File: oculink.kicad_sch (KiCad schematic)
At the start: 15 parts, among them J6 OCuLink_x4_Amphenol_G14A42121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

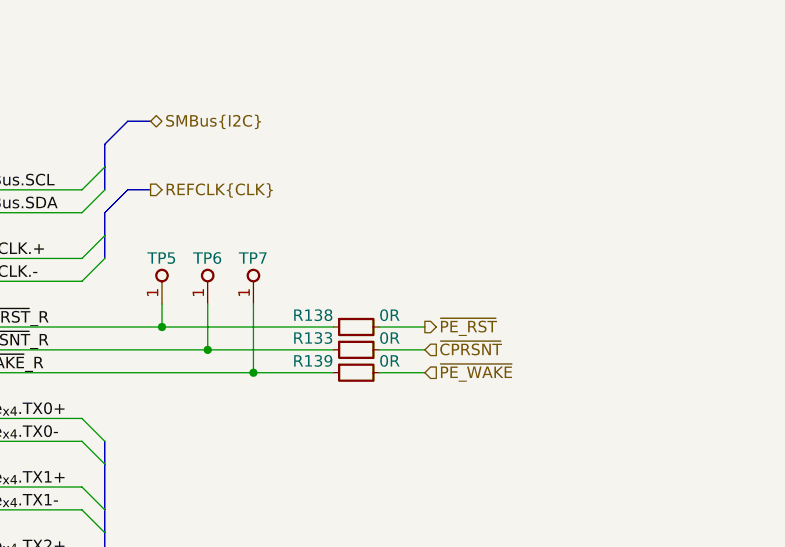
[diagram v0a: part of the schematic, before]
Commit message: [#85196] WIP: Add power sequencing, connect CPRSNT signal
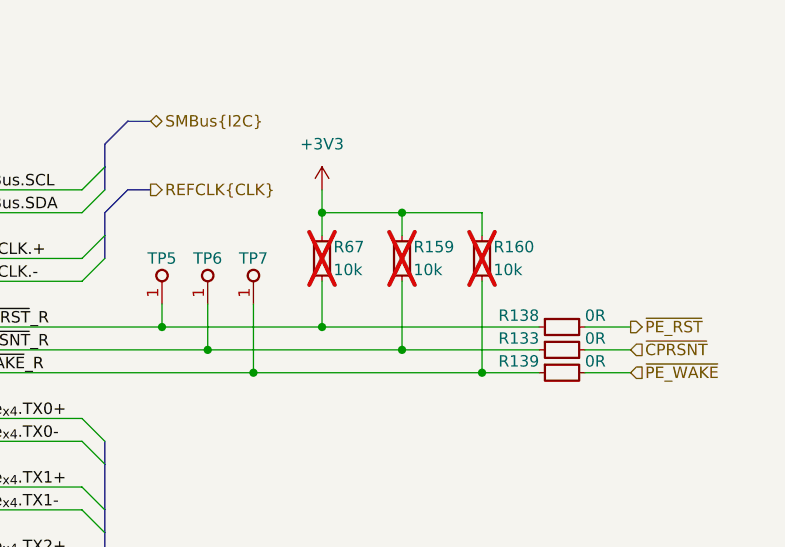
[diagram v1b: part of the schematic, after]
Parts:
- added R159, R160, R67: R_10k_0402, antmicro-footprints:R_0402_1005Metric, symbol antmicroResistors0402:R_10k_0402
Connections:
- net ~{CPRSNT}_R: now also R159.1
- net ~{CWAKE}_R: now also R160.1
- net ~{PE_ RST}_R: now also R67.1
- new net +3V3: R159.2, R160.2, R67.2
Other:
- moved on the sheet: R133, R138, R139

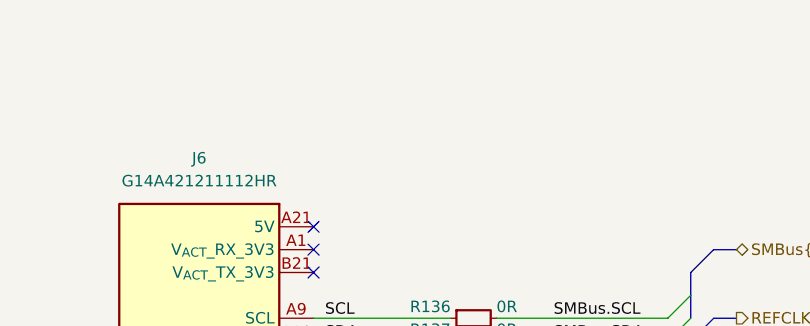
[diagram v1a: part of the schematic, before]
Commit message: [#85196] Clear ERC, minor schematic fixes
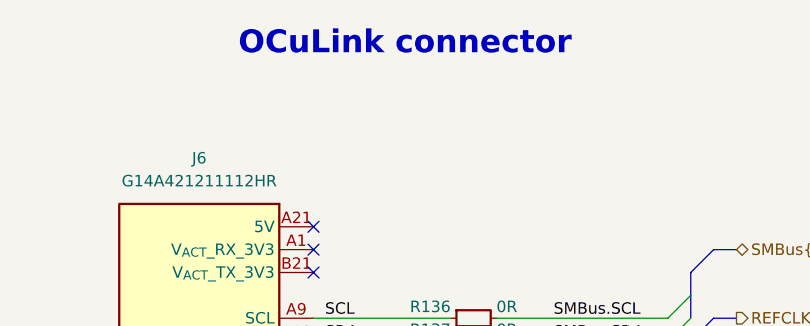
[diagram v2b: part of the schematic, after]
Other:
- note added: "OCuLink connector"
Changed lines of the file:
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@@
 		(comment 1 "www.antmicro.com")
+	)
+	(text "OCuLink connector"
+		(exclude_from_sim no)
+		(at 201.93 64.77 0)
+		(effects
+			(font
+				(size 2.54 2.54)
+				(thickness 0.508)
+				(bold yes)
+			)
+		)
 	)
 	(junction

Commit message: [#85196] Re-annotate schematic
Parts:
- renumbered D1 to D4, D3 to D6, D4 to D7, D2 to D8, D6 to D9, J6 to J9, R136 to R162, R137 to R163, R67 to R164, R159 to R165, R160 to R166, R138 to R167, R133 to R168, R139 to R169, TP5 to TP14, TP6 to TP15, TP7 to TP16
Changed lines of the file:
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@@
 		(on_board yes)
 		(dnp yes)
-		(property "Reference" "R160"
+		(property "Reference" "R166"
 			(at 276.86 101.6 90)
 			(effects
@@
 			(project "10-gbe-expansion"
 				(path "/04bda987-e5eb-48b4-9e90-d8211dc11b39/0cbe4665-19ed-43d5-9283-363c2bb680b6"
-					(reference "R160")
+					(reference "R166")
 					(unit 1)
 				)
@@
 		(dnp no)
 		(fields_autoplaced yes)
-		(property "Reference" "D2"
+		(property "Reference" "D8"
 			(at 222.25 238.76 0)
 			(effects
@@
 			(project "10-gbe-expansion"
 				(path "/04bda987-e5eb-48b4-9e90-d8211dc11b39/0cbe4665-19ed-43d5-9283-363c2bb680b6"
-					(reference "D2")
+					(reference "D8")
 					(unit 1)
 				)
@@
 		(on_board yes)
 		(dnp no)
-		(property "Reference" "R139"
+		(property "Reference" "R169"
 			(at 281.94 114.3 0)
 			(effects
@@
 			(project ""
 				(path "/04bda987-e5eb-48b4-9e90-d8211dc11b39/0cbe4665-19ed-43d5-9283-363c2bb680b6"
-					(reference "R139")
+					(reference "R169")
 					(unit 1)
 				)
@@
 		(on_board yes)
 		(dnp no)
-		(property "Reference" "R136"
+		(property "Reference" "R162"
 			(at 207.01 93.98 0)
 			(effects
@@
 			(project "10-gbe-expansion"
 				(path "/04bda987-e5eb-48b4-9e90-d8211dc11b39/0cbe4665-19ed-43d5-9283-363c2bb680b6"
-					(reference "R136")
+					(reference "R162")
 					(unit 1)
 				)
@@
 		(dnp no)
 		(fields_autoplaced yes)
-		(property "Reference" "D6"
+		(property "Reference" "D9"
 			(at 271.78 238.76 0)
 			(effects
@@
 			(project "10-gbe-expansion"
 				(path "/04bda987-e5eb-48b4-9e90-d8211dc11b39/0cbe4665-19ed-43d5-9283-363c2bb680b6"
-					(reference "D6")
+					(reference "D9")
 					(unit 1)
 				)
@@
 		(on_board yes)
 		(dnp yes)
-		(property "Reference" "R67"
+		(property "Reference" "R164"
 			(at 259.08 101.6 90)
 			(effects
@@
 			(project ""
 				(path "/04bda987-e5eb-48b4-9e90-d8211dc11b39/0cbe4665-19ed-43d5-9283-363c2bb680b6"
-					(reference "R67")
+					(reference "R164")
 					(unit 1)
 				)
@@
 		(on_board yes)
 		(dnp no)
-		(property "Reference" "#PWR0268"
+		(property "Reference" "#PWR0322"
 			(at 167.64 224.79 0)
 			(effects
@@
 			(project "10-gbe-expansion"
 				(path "/04bda987-e5eb-48b4-9e90-d8211dc11b39/0cbe4665-19ed-43d5-9283-363c2bb680b6"
-					(reference "#PWR0268")
+					(reference "#PWR0322")
 					(unit 1)
 				)
@@
 		(dnp no)
 		(fields_autoplaced yes)
-		(property "Reference" "D1"
+		(property "Reference" "D4"
 			(at 171.45 213.36 0)
 			(effects
@@
 			(project "10-gbe-expansion"
 				(path "/04bda987-e5eb-48b4-9e90-d8211dc11b39/0cbe4665-19ed-43d5-9283-363c2bb680b6"
-					(reference "D1")
+					(reference "D4")
 					(unit 1)
 				)
@@
 		(dnp no)
 		(fields_autoplaced yes)
-		(property "Reference" "#PWR0315"
+		(property "Reference" "#PWR0320"
 			(at 273.05 95.25 0)
 			(effects
@@
 			(project ""
 				(path "/04bda987-e5eb-48b4-9e90-d8211dc11b39/0cbe4665-19ed-43d5-9283-363c2bb680b6"
-					(reference "#PWR0315")
+					(reference "#PWR0320")
 					(unit 1)
 				)
@@
 		(on_board yes)
 		(dnp no)
-		(property "Reference" "#PWR0270"
+		(property "Reference" "#PWR0324"
 			(at 267.97 224.79 0)
 			(effects
@@
 			(project "10-gbe-expansion"
 				(path "/04bda987-e5eb-48b4-9e90-d8211dc11b39/0cbe4665-19ed-43d5-9283-363c2bb680b6"
-					(reference "#PWR0270")
+					(reference "#PWR0324")
 					(unit 1)
 				)
@@
 		(dnp no)
 		(fields_autoplaced yes)
-		(property "Reference" "D3"
+		(property "Reference" "D6"
 			(at 271.78 213.36 0)
 			(effects
@@
 			(project "10-gbe-expansion"
 				(path "/04bda987-e5eb-48b4-9e90-d8211dc11b39/0cbe4665-19ed-43d5-9283-363c2bb680b6"
-					(reference "D3")
+					(reference "D6")
 					(unit 1)
 				)
@@
 		(on_board yes)
 		(dnp no)
-		(property "Reference" "TP5"
+		(property "Reference" "TP14"
 			(at 240.03 102.87 90)
 			(effects
@@
 			(project ""
 				(path "/04bda987-e5eb-48b4-9e90-d8211dc11b39/0cbe4665-19ed-43d5-9283-363c2bb680b6"
-					(reference "TP5")
+					(reference "TP14")
 					(unit 1)
 				)
@@
 		(dnp no)
 		(fields_autoplaced yes)
-		(property "Reference" "J6"
+		(property "Reference" "J9"
 			(at 179.07 77.47 0)
 			(effects
@@
 			(project ""
 				(path "/04bda987-e5eb-48b4-9e90-d8211dc11b39/0cbe4665-19ed-43d5-9283-363c2bb680b6"
-					(reference "J6")
+					(reference "J9")
 					(unit 1)
 				)
@@
 		(on_board yes)
 		(dnp no)
-		(property "Reference" "#PWR0271"
+		(property "Reference" "#PWR0321"
 			(at 172.72 181.61 0)
 			(effects
@@
 			(project "10-gbe-expansion"
 				(path "/04bda987-e5eb-48b4-9e90-d8211dc11b39/0cbe4665-19ed-43d5-9283-363c2bb680b6"
-					(reference "#PWR0271")
+					(reference "#PWR0321")
 					(unit 1)
 				)
@@
 		(on_board yes)
 		(dnp no)
-		(property "Reference" "R137"
+		(property "Reference" "R163"
 			(at 207.01 96.52 0)
 			(effects
@@
 			(project "10-gbe-expansion"
 				(path "/04bda987-e5eb-48b4-9e90-d8211dc11b39/0cbe4665-19ed-43d5-9283-363c2bb680b6"
-					(reference "R137")
+					(reference "R163")
 					(unit 1)
 				)
@@
 		(on_board yes)
 		(dnp no)
-		(property "Reference" "R138"
+		(property "Reference" "R167"
 			(at 281.94 109.22 0)
 			(effects
@@
 			(project "10-gbe-expansion"
 				(path "/04bda987-e5eb-48b4-9e90-d8211dc11b39/0cbe4665-19ed-43d5-9283-363c2bb680b6"
-					(reference "R138")
+					(reference "R167")
 					(unit 1)
 				)
@@
 		(on_board yes)
 		(dnp no)
-		(property "Reference" "#PWR0269"
+		(property "Reference" "#PWR0326"
 			(at 218.44 250.19 0)
 			(effects
@@
 			(project "10-gbe-expansion"
 				(path "/04bda987-e5eb-48b4-9e90-d8211dc11b39/0cbe4665-19ed-43d5-9283-363c2bb680b6"
-					(reference "#PWR0269")
+					(reference "#PWR0326")
 					(unit 1)
 				)
@@
 		(on_board yes)
 		(dnp no)
-		(property "Reference" "TP6"
+		(property "Reference" "TP15"
 			(at 245.11 102.87 90)
 			(effects
@@
 			(project "10-gbe-expansion"
 				(path "/04bda987-e5eb-48b4-9e90-d8211dc11b39/0cbe4665-19ed-43d5-9283-363c2bb680b6"
-					(reference "TP6")
+					(reference "TP15")
 					(unit 1)
 				)
@@
 		(on_board yes)
 		(dnp no)
-		(property "Reference" "#PWR0274"
+		(property "Reference" "#PWR0327"
 			(at 267.97 250.19 0)
 			(effects
@@
 			(project "10-gbe-expansion"
 				(path "/04bda987-e5eb-48b4-9e90-d8211dc11b39/0cbe4665-19ed-43d5-9283-363c2bb680b6"
-					(reference "#PWR0274")
+					(reference "#PWR0327")
 					(unit 1)
 				)
@@
 		(dnp no)
 		(fields_autoplaced yes)
-		(property "Reference" "D4"
+		(property "Reference" "D7"
 			(at 171.45 238.76 0)
 			(effects
@@
 			(project ""
 				(path "/04bda987-e5eb-48b4-9e90-d8211dc11b39/0cbe4665-19ed-43d5-9283-363c2bb680b6"
-					(reference "D4")
+					(reference "D7")
 					(unit 1)
 				)
@@
 		(on_board yes)
 		(dnp yes)
-		(property "Reference" "R159"
+		(property "Reference" "R165"
 			(at 267.97 101.6 90)
 			(effects
@@
 			(project "10-gbe-expansion"
 				(path "/04bda987-e5eb-48b4-9e90-d8211dc11b39/0cbe4665-19ed-43d5-9283-363c2bb680b6"
-					(reference "R159")
+					(reference "R165")
 					(unit 1)
 				)
@@
 		(on_board yes)
 		(dnp no)
-		(property "Reference" "#PWR0273"
+		(property "Reference" "#PWR0323"
 			(at 218.44 224.79 0)
 			(effects
@@
 			(project "10-gbe-expansion"
 				(path "/04bda987-e5eb-48b4-9e90-d8211dc11b39/0cbe4665-19ed-43d5-9283-363c2bb680b6"
-					(reference "#PWR0273")
+					(reference "#PWR0323")
 					(unit 1)
 				)
@@
 		(on_board yes)
 		(dnp no)
-		(property "Reference" "#PWR0272"
+		(property "Reference" "#PWR0325"
 			(at 167.64 250.19 0)
 			(effects
@@
 			(project "10-gbe-expansion"
 				(path "/04bda987-e5eb-48b4-9e90-d8211dc11b39/0cbe4665-19ed-43d5-9283-363c2bb680b6"
-					(reference "#PWR0272")
+					(reference "#PWR0325")
 					(unit 1)
 				)
@@
 		(on_board yes)
 		(dnp no)
-		(property "Reference" "R133"
+		(property "Reference" "R168"
 			(at 281.94 111.76 0)
 			(effects
@@
 			(project "10-gbe-expansion"
 				(path "/04bda987-e5eb-48b4-9e90-d8211dc11b39/0cbe4665-19ed-43d5-9283-363c2bb680b6"
-					(reference "R133")
+					(reference "R168")
 					(unit 1)
 				)
@@
 		(on_board yes)
 		(dnp no)
-		(property "Reference" "TP7"
+		(property "Reference" "TP16"
 			(at 250.19 102.87 90)
 			(effects
@@
 			(project "10-gbe-expansion"
 				(path "/04bda987-e5eb-48b4-9e90-d8211dc11b39/0cbe4665-19ed-43d5-9283-363c2bb680b6"
-					(reference "TP7")
+					(reference "TP16")
 					(unit 1)
 				)
